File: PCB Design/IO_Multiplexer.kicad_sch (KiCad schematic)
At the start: 17 parts, among them J42 Conn_Sig, J43 Conn_I2C, J45 Conn_01x04_Pin, J46 Conn_I2C, J47 Conn, U41 AMS1117-3.3, U42 SX1509BIULTRT, U43 TCA9406DC

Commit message: Minor Improvements
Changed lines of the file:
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@@
+	(wire
+		(pts
+			(xy 259.08 160.02) (xy 261.62 160.02)
+		)
+		(stroke
+			(width 0)
+			(type default)
+		)
+	)
 	(wire
 		(pts
@@
 		(pts
 			(xy 106.68 119.38) (xy 109.22 119.38)
+		)
+		(stroke
+			(width 0)
+			(type default)
+		)
+	)
+	(wire
+		(pts
+			(xy 259.08 156.21) (xy 261.62 156.21)
 		)
 		(stroke
@@
 		)
 	)
+	(label "VExt"
+		(at 259.08 160.02 180)
+		(fields_autoplaced yes)
+		(effects
+			(font
+				(size 1.27 1.27)
+			)
+			(justify right bottom)
+		)
+	)
 	(label "SCL_VCC"
 		(at 248.92 41.91 180)
@@
 			)
 			(justify left bottom)
+		)
+	)
+	(label "GND"
+		(at 259.08 156.21 180)
+		(fields_autoplaced yes)
+		(effects
+			(font
+				(size 1.27 1.27)
+			)
+			(justify right bottom)
 		)
 	)
@@
 	)
 	(symbol
+		(lib_id "power:PWR_FLAG")
+		(at 261.62 156.21 270)
+		(unit 1)
+		(exclude_from_sim no)
+		(in_bom yes)
+		(on_board yes)
+		(dnp no)
+		(fields_autoplaced yes)
+		(property "Reference" "#FLG041"
+			(at 263.525 156.21 0)
+			(effects
+				(font
+					(size 1.27 1.27)
+				)
+				(hide yes)
+			)
+		)
+		(property "Value" "PWR_FLAG"
+			(at 265.43 156.2099 90)
+			(effects
+				(font
+					(size 1.27 1.27)
+				)
+				(justify left)
+			)
+		)
+		(property "Footprint" ""
+			(at 261.62 156.21 0)
+			(effects
+				(font
+					(size 1.27 1.27)
+				)
+				(hide yes)
+			)
+		)
+		(property "Datasheet" "~"
+			(at 261.62 156.21 0)
+			(effects
+				(font
+					(size 1.27 1.27)
+				)
+				(hide yes)
+			)
+		)
+		(property "Description" "Special symbol for telling ERC where power comes from"
+			(at 261.62 156.21 0)
+			(effects
+				(font
+					(size 1.27 1.27)
+				)
+				(hide yes)
+			)
+		)
+		(pin "1"
+		)
+		(instances
+			(project "Vending_Machine"
+				(path "/061ecb1c-afb0-4b5f-8f93-1c1ad8e1529c/9c3cb50a-c3f7-4dce-9b4b-c52119142b1e"
+					(reference "#FLG041")
+					(unit 1)
+				)
+			)
+		)
+	)
+	(symbol
 		(lib_id "Device:C_Small")
 		(at 200.66 45.72 0)
@@
 					(unit 1)
 				)
+			)
+		)
+	)
+	(symbol
+		(lib_id "power:PWR_FLAG")
+		(at 261.62 160.02 270)
+		(unit 1)
+		(exclude_from_sim no)
+		(in_bom yes)
+		(on_board yes)
+		(dnp no)
+		(fields_autoplaced yes)
+		(property "Reference" "#FLG042"
+			(at 263.525 160.02 0)
+			(effects
+				(font
+					(size 1.27 1.27)
+				)
+				(hide yes)
+			)
+		)
+		(property "Value" "PWR_FLAG"
+			(at 265.43 160.0199 90)
+			(effects
+				(font
+					(size 1.27 1.27)
+				)
+				(justify left)
+			)
+		)
+		(property "Footprint" ""
+			(at 261.62 160.02 0)
+			(effects
+				(font
+					(size 1.27 1.27)
+				)
+				(hide yes)
+			)
+		)
+		(property "Datasheet" "~"
+			(at 261.62 160.02 0)
+			(effects
+				(font
+					(size 1.27 1.27)
+				)
+				(hide yes)
+			)
+		)
+		(property "Description" "Special symbol for telling ERC where power comes from"
+			(at 261.62 160.02 0)
+			(effects
+				(font
+					(size 1.27 1.27)
+				)
+				(hide yes)
+			)
+		)
+		(pin "1"
+		)
+		(instances
+			(project "Vending_Machine"
+				(path "/061ecb1c-afb0-4b5f-8f93-1c1ad8e1529c/9c3cb50a-c3f7-4dce-9b4b-c52119142b1e"
+					(reference "#FLG042")
+					(unit 1)
+				)

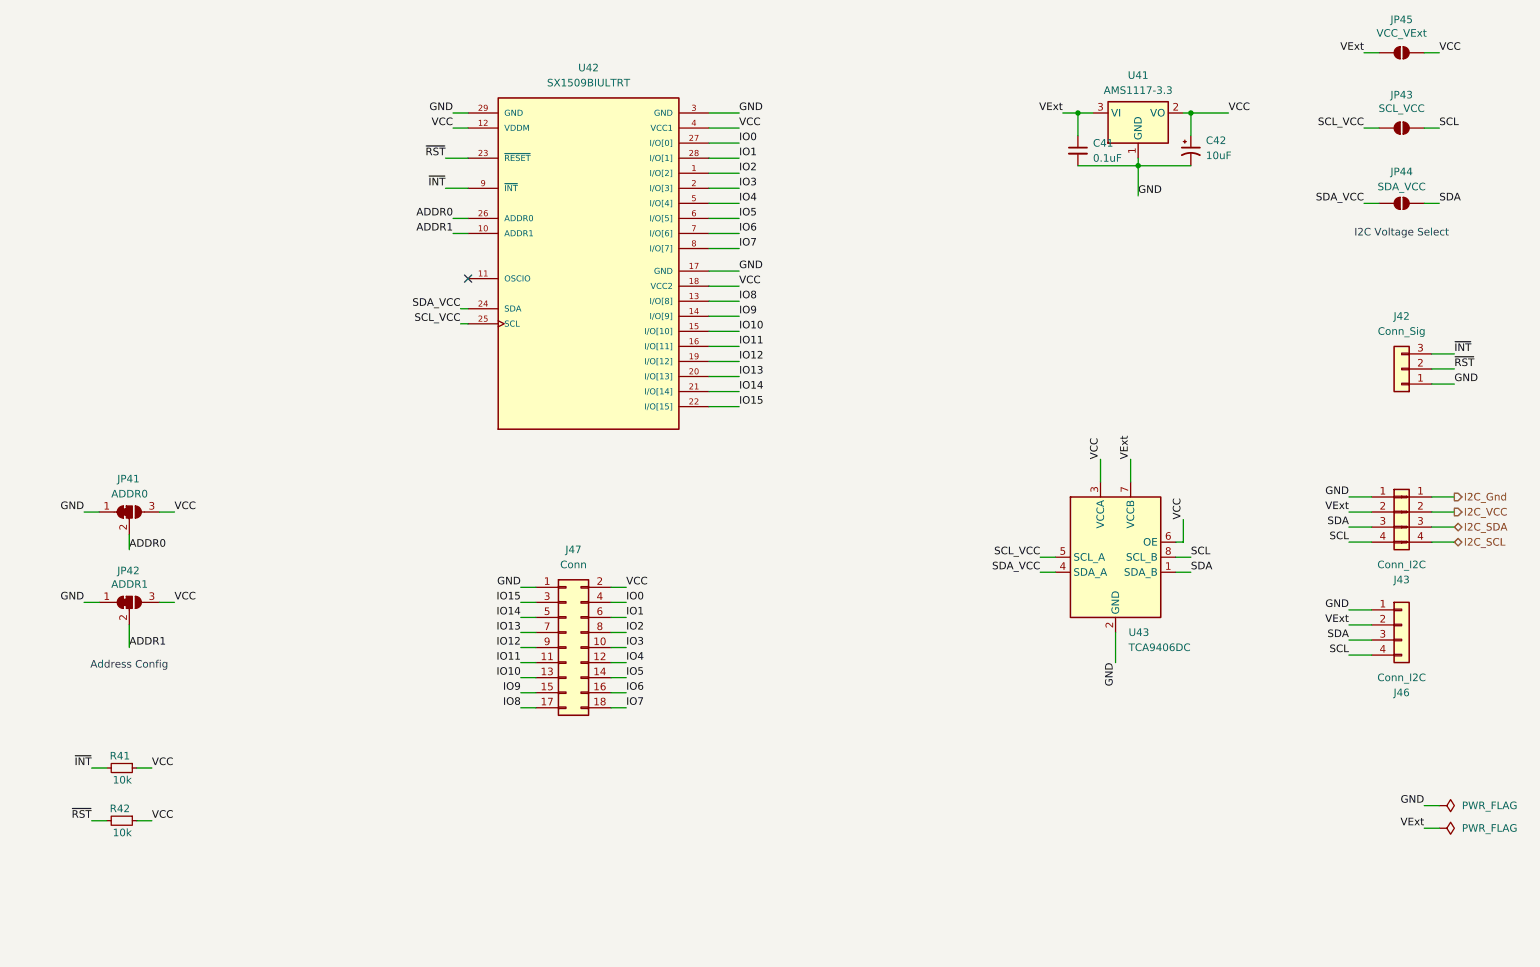
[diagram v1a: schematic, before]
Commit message: Tweaks and Updates
Added OSCIO pin to breakout board.
A few more tweaks
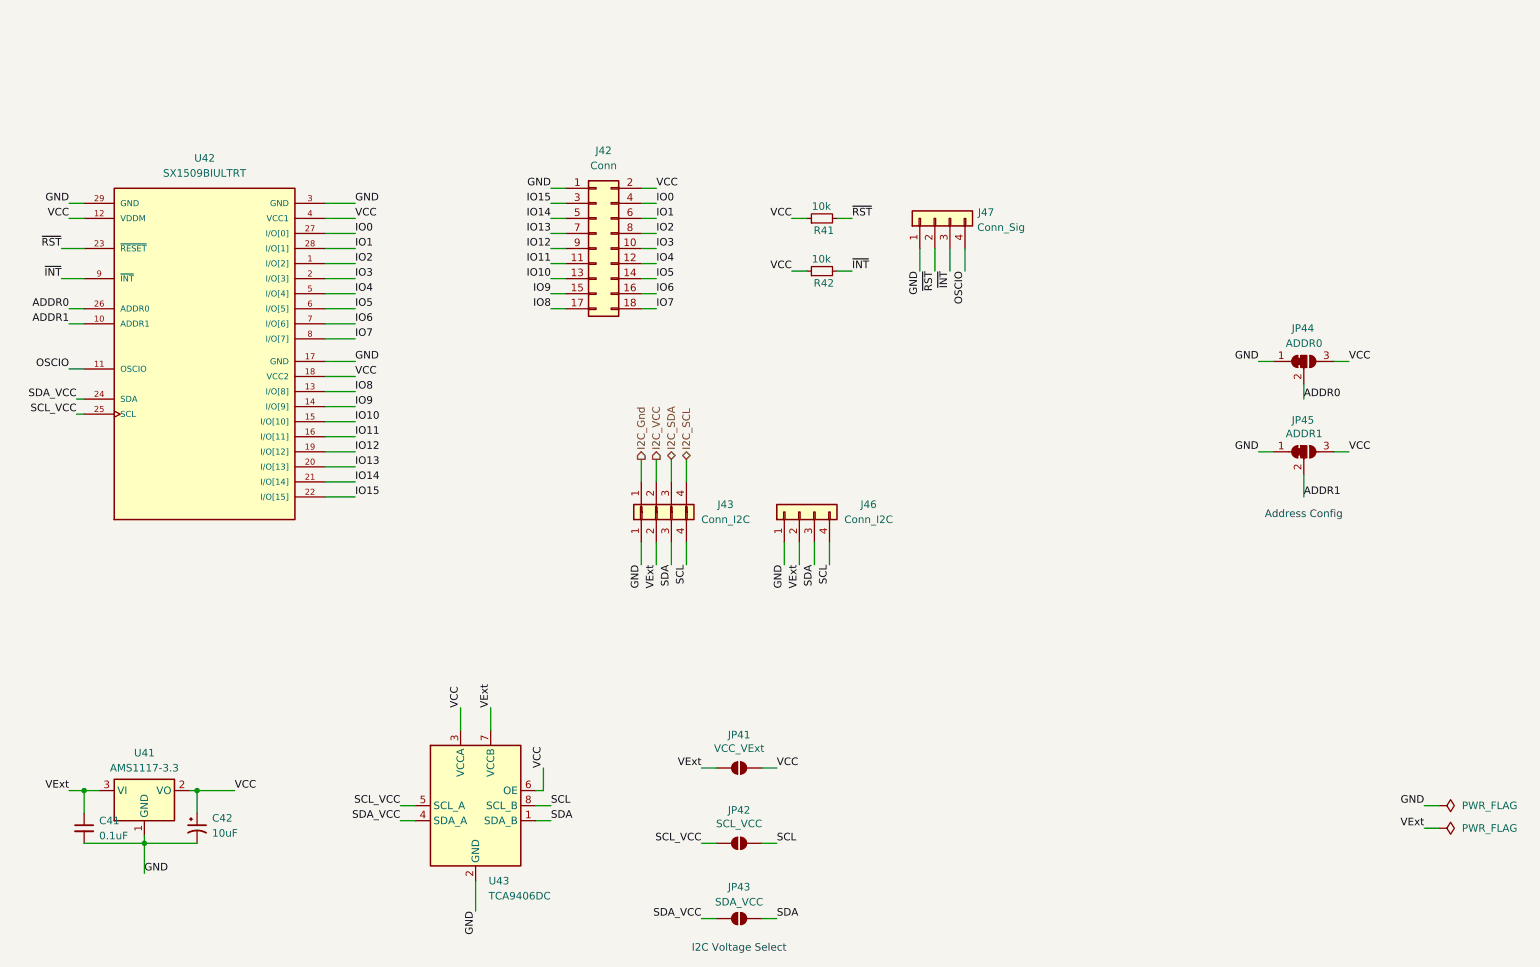
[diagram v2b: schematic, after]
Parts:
- J47: renamed from J42; footprint Connector_JST:JST_XH_B3B-XH-A_1x03_P2.50mm_Vertical -> Connector_JST:JST_XH_B4B-XH-A_1x04_P2.50mm_Vertical; symbol Connector_Generic:Conn_01x03 -> Connector_Generic:Conn_01x04
- renumbered J47 to J42, JP45 to JP41, JP43 to JP42, JP44 to JP43, JP41 to JP44, JP42 to JP45, R42 to R41, R41 to R42
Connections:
- net OSCIO: now reaches U42.11 (OSCIO)
- net OSCIO: now also J47.4 (Pin_4)
- no-connect marks 1 -> 0
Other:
- moved on the sheet: C41, C42, J42, J43, J46, JP41, JP42, JP43, JP44, JP45, R41, R42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

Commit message: Testpoints to schematic.
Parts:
- added TP39, TP48, TP58: VCC, Footprints:TestPoint_Pad_D1.0mm, symbol Connector:TestPoint_Small
- added TP40: ~{RST}, Footprints:TestPoint_Pad_D1.0mm, symbol Connector:TestPoint_Small
- added TP41: ~{INT}, Footprints:TestPoint_Pad_D1.0mm, symbol Connector:TestPoint_Small
- added TP42: Addr0, Footprints:TestPoint_Pad_D1.0mm, symbol Connector:TestPoint_Small
- added TP43: Addr1, Footprints:TestPoint_Pad_D1.0mm, symbol Connector:TestPoint_Small
- added TP44: OSC, Footprints:TestPoint_Pad_D1.0mm, symbol Connector:TestPoint_Small
- added TP45: SDA, Footprints:TestPoint_Pad_D1.0mm, symbol Connector:TestPoint_Small
- added TP46: SCL, Footprints:TestPoint_Pad_D1.0mm, symbol Connector:TestPoint_Small
- added TP47, TP57: GND, Footprints:TestPoint_Pad_D1.0mm, symbol Connector:TestPoint_Small
- added TP49: IO0, Footprints:TestPoint_Pad_D1.0mm, symbol Connector:TestPoint_Small
- added TP50: IO1, Footprints:TestPoint_Pad_D1.0mm, symbol Connector:TestPoint_Small
- added TP51: IO2, Footprints:TestPoint_Pad_D1.0mm, symbol Connector:TestPoint_Small
- added TP52: IO3, Footprints:TestPoint_Pad_D1.0mm, symbol Connector:TestPoint_Small
- added TP53: IO4, Footprints:TestPoint_Pad_D1.0mm, symbol Connector:TestPoint_Small
- added TP54: IO5, Footprints:TestPoint_Pad_D1.0mm, symbol Connector:TestPoint_Small
- added TP55: IO6, Footprints:TestPoint_Pad_D1.0mm, symbol Connector:TestPoint_Small
- added TP56: IO7, Footprints:TestPoint_Pad_D1.0mm, symbol Connector:TestPoint_Small
- added TP59: IO8, Footprints:TestPoint_Pad_D1.0mm, symbol Connector:TestPoint_Small
- added TP60: IO9, Footprints:TestPoint_Pad_D1.0mm, symbol Connector:TestPoint_Small
- added TP61: IO10, Footprints:TestPoint_Pad_D1.0mm, symbol Connector:TestPoint_Small
- added TP62: IO11, Footprints:TestPoint_Pad_D1.0mm, symbol Connector:TestPoint_Small
- added TP63: IO12, Footprints:TestPoint_Pad_D1.0mm, symbol Connector:TestPoint_Small
- added TP64: IO13, Footprints:TestPoint_Pad_D1.0mm, symbol Connector:TestPoint_Small
- added TP65: IO14, Footprints:TestPoint_Pad_D1.0mm, symbol Connector:TestPoint_Small
- added TP66: IO15, Footprints:TestPoint_Pad_D1.0mm, symbol Connector:TestPoint_Small
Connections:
- net ADDR0: now also TP42.1
- net ADDR1: now also TP43.1
- net GND: now also TP47.1, TP57.1
- net IO0: now also TP49.1
- net IO1: now also TP50.1
- net IO10: now also TP61.1
- net IO11: now also TP62.1
- net IO12: now also TP63.1
- net IO13: now also TP64.1
- net IO14: now also TP65.1
- net IO15: now also TP66.1
- net IO2: now also TP51.1
- net IO3: now also TP52.1
- net IO4: now also TP53.1
- net IO5: now also TP54.1
- net IO6: now also TP55.1
- net IO7: now also TP56.1
- net IO8: now also TP59.1
- net IO9: now also TP60.1
- net OSCIO: now also TP44.1
- net SCL_VCC: now also TP46.1
- net SDA_VCC: now also TP45.1
- net VCC: now also TP39.1, TP48.1, TP58.1
- net ~{INT}: now also TP41.1
- net ~{RST}: now also TP40.1

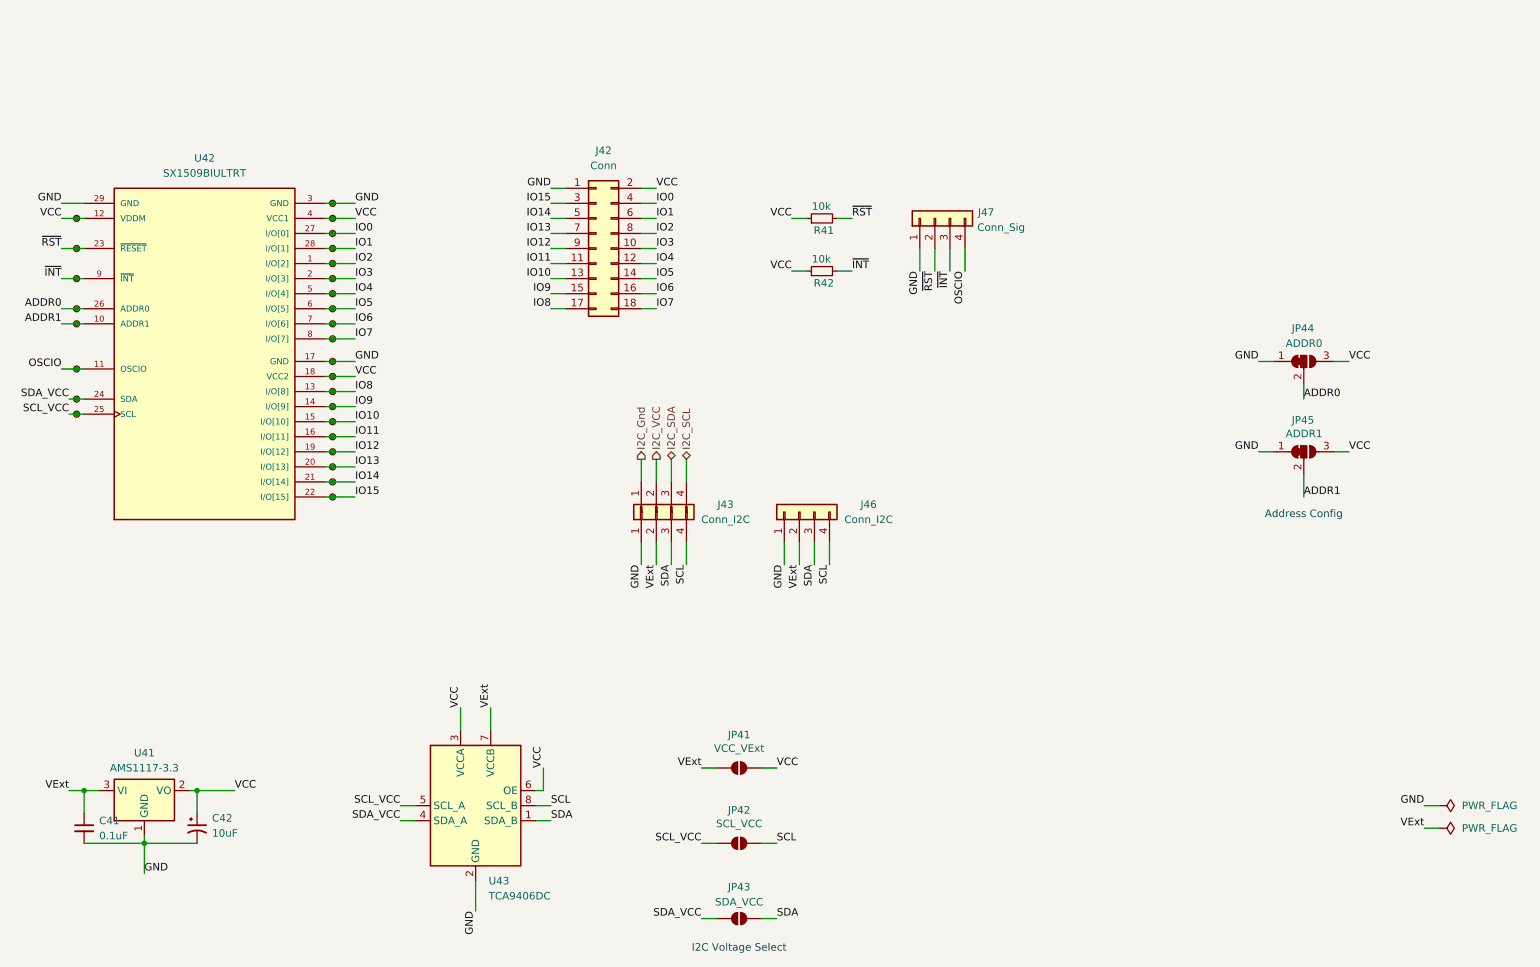
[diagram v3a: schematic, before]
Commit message: Vcc->3v3 Added extra GPIO
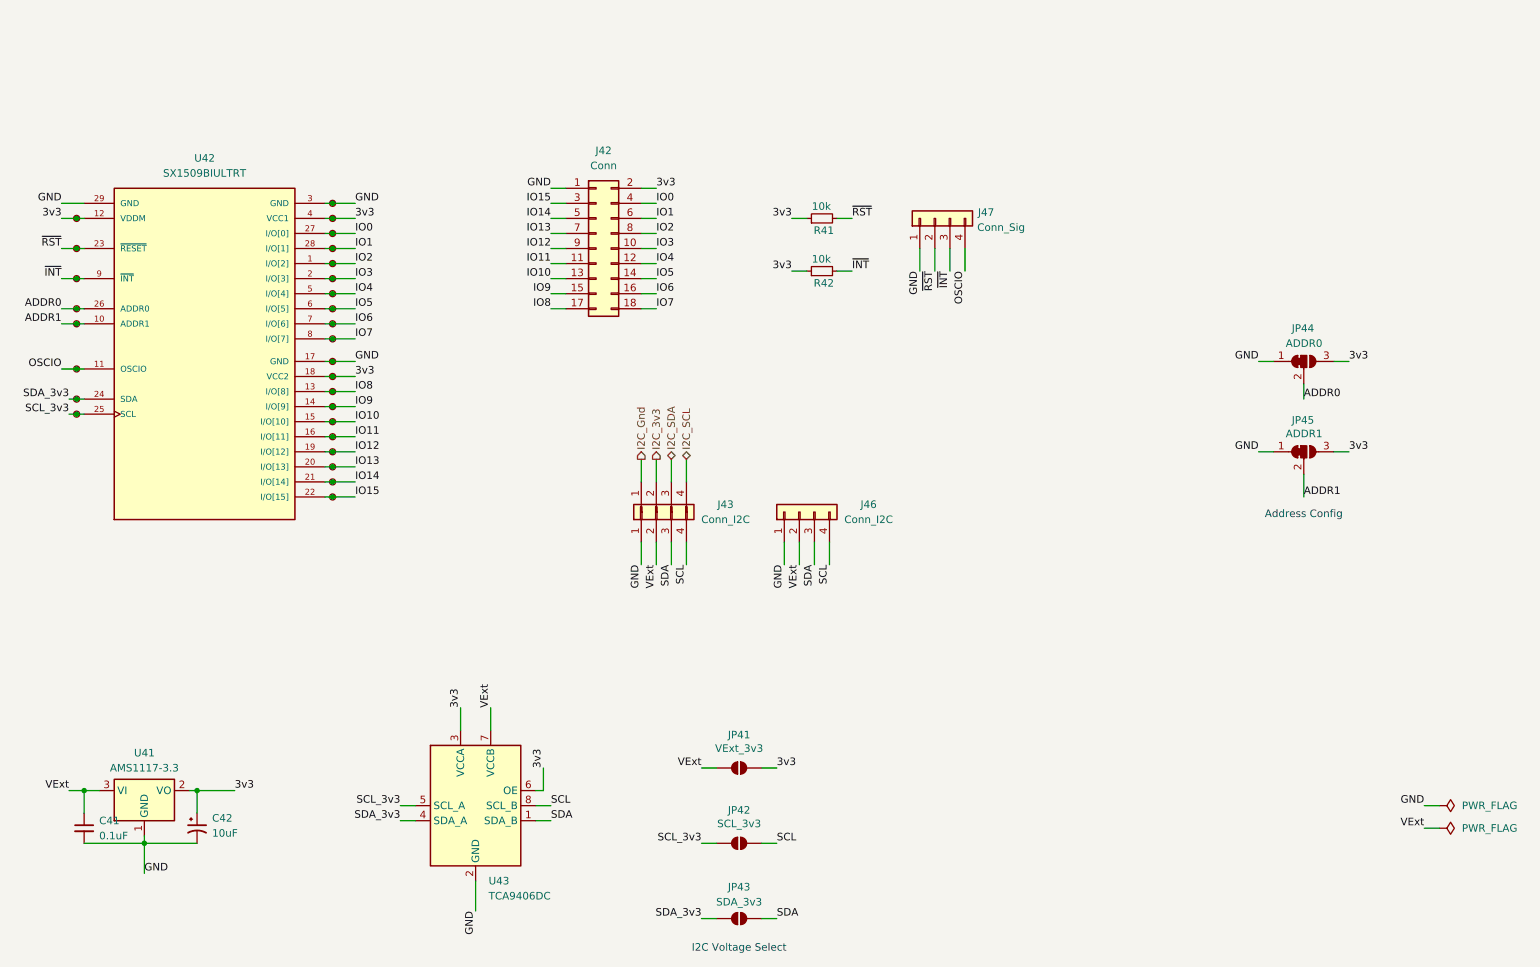
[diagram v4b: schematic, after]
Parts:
- JP41: value VCC_VExt -> VExt_3v3
- JP42: value SCL_VCC -> SCL_3v3
- JP43: value SDA_VCC -> SDA_3v3
- TP39, TP48, TP58: value VCC -> 3v3
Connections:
- net I2C_VCC renamed I2C_3v3
- net SCL_VCC renamed SCL_3v3
- net SDA_VCC renamed SDA_3v3
- net VCC renamed 3v3
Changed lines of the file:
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@@
 		)
 	)
-	(label "SDA_VCC"
+	(label "SDA_3v3"
 		(at 30.48 87.63 180)
 		(fields_autoplaced yes)
@@
 		)
 	)
-	(label "SCL_VCC"
+	(label "SCL_3v3"
 		(at 137.16 162.56 180)
 		(fields_autoplaced yes)
@@
 		)
 	)
-	(label "SCL_VCC"
+	(label "SCL_3v3"
 		(at 86.36 156.21 180)
 		(fields_autoplaced yes)
@@
 		)
 	)
-	(label "VCC"
+	(label "3v3"
 		(at 246.38 96.52 0)
 		(fields_autoplaced yes)
@@
 		)
 	)
-	(label "VCC"
+	(label "3v3"
 		(at 78.74 57.15 0)
 		(fields_autoplaced yes)
@@
 		)
 	)
-	(label "VCC"
+	(label "3v3"
 		(at 129.54 52.07 0)
 		(fields_autoplaced yes)
@@
 		)
 	)
-	(label "SCL_VCC"
+	(label "SCL_3v3"
 		(at 30.48 90.17 180)
 		(fields_autoplaced yes)
@@
 		)
 	)
-	(label "VCC"
+	(label "3v3"
 		(at 246.38 81.28 0)
 		(fields_autoplaced yes)
@@
 		)
 	)
-	(label "SDA_VCC"
+	(label "SDA_3v3"
 		(at 137.16 175.26 180)
 		(fields_autoplaced yes)
@@
 		)
 	)
-	(label "VCC"
+	(label "3v3"
 		(at 110.49 149.86 90)
 		(fields_autoplaced yes)
@@
 		)
 	)
-	(label "VCC"
+	(label "3v3"
 		(at 152.4 66.04 180)
 		(fields_autoplaced yes)
@@
 		)
 	)
-	(label "VCC"
+	(label "3v3"
 		(at 96.52 139.7 90)
 		(fields_autoplaced yes)
@@
 		)
 	)
-	(label "VCC"
+	(label "3v3"
 		(at 152.4 57.15 180)
 		(fields_autoplaced yes)
@@
 		)
 	)
-	(label "VCC"
+	(label "3v3"
 		(at 29.21 57.15 180)
 		(fields_autoplaced yes)
@@
 		)
 	)
-	(label "VCC"
+	(label "3v3"
 		(at 58.42 153.67 0)
 		(fields_autoplaced yes)
@@
 		)
 	)
-	(label "VCC"
+	(label "3v3"
 		(at 149.86 149.86 0)
 		(fields_autoplaced yes)
@@
 		)
 	)
-	(label "SDA_VCC"
+	(label "SDA_3v3"
 		(at 86.36 158.75 180)
 		(fields_autoplaced yes)
@@
 		)
 	)
-	(label "VCC"
+	(label "3v3"
 		(at 78.74 83.82 0)
 		(fields_autoplaced yes)
@@
 		)
 	)
-	(hierarchical_label "I2C_VCC"
+	(hierarchical_label "I2C_3v3"
 		(shape output)
 		(at 129.54 97.79 90)
@@
 			)
 		)
-		(property "Value" "VCC"
+		(property "Value" "3v3"
 			(at 33.02 58.4199 0)
 			(effects
@@
 			)
 		)
-		(property "Value" "VCC_VExt"
+		(property "Value" "VExt_3v3"
 			(at 143.51 146.558 0)
 			(effects
@@
 			)
 		)
-		(property "Value" "SCL_VCC"
+		(property "Value" "SCL_3v3"
 			(at 143.51 159.258 0)
 			(effects
@@
 			)
 		)
-		(property "Value" "VCC"
+		(property "Value" "3v3"
 			(at 76.2 58.4199 0)
 			(effects
@@
 			)
 		)
-		(property "Value" "SDA_VCC"
+		(property "Value" "SDA_3v3"
 			(at 143.51 172.466 0)
 			(effects
@@
 			)
 		)
-		(property "Value" "VCC"
+		(property "Value" "3v3"
 			(at 76.2 85.0899 0)
 			(effects
